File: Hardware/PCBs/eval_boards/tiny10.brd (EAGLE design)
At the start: 12.7 x 17.7 mm, 5 parts, among them IC1 HSDL-9100

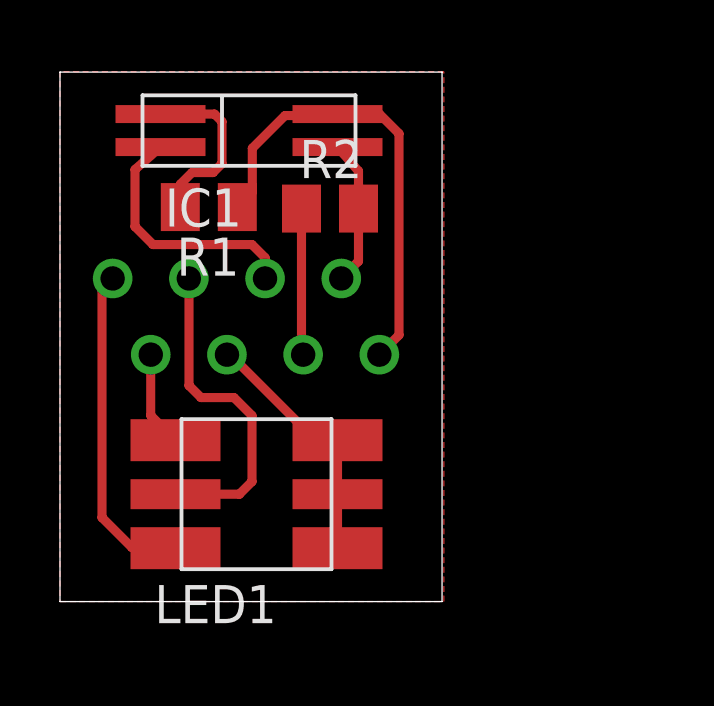
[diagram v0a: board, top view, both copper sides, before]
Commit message: the forgotten commit ;)
* enhance bottom, rgb sensor pcb
* create attiny and lm239 eval boards
* bug fix for the pdf export scripts
* correct attiny soft power switch simulation
* add experimental color sensor code
* add rgb color look up table
* correct motor roations
* various other (this is the forgetten commit)
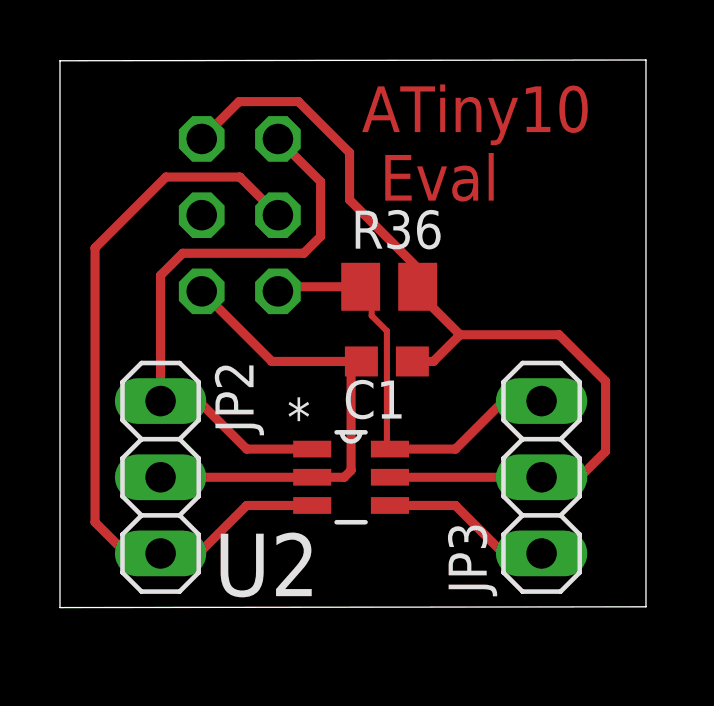
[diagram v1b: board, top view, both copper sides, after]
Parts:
- removed IC1: HSDL-9100, BEEP:HSDL-9100
- removed LED1: F503605050, BEEP:5050LED
- removed R1: (no value), resistor:M0805
- removed R2: 39K, resistor:M0805
- removed X1: (no value), con-amp:FTOP-8
- added C1: 100n, rcl:C0603
- added JP1: (no value), pinhead:2X03
- added JP2, JP3: (no value), pinhead:1X03
- added R36: (no value), rcl:M0805
- added U2: ATTINY10-TSHR, Atmel_By_element14_Batch_1:SOT95P280X145-6N
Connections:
- removed net +5V: IC1.DET_K, R1.1, X1.1
- removed net ADISTANCE: IC1.DET_A, R2.2, X1.2
- removed net IR_LED_K: IC1.LED_K, X1.4
- removed net N$2: IC1.LED_A, R1.2
- removed net RGB_ANODE_1: LED1.B1, X1.8
- removed net RGB_ANODE_2: LED1.G1, X1.6
- removed net RGB_ANODE_3: LED1.R1, X1.7
- removed net RGB_COMMON_K: LED1.B2, LED1.G2, LED1.R2, X1.5
- new net +3V3: C1.1, JP1.2, JP3.2, R36.2, U2.5
- new net PB0/TPIDATA: JP1.1, JP2.1, U2.1
- new net PB1/TPICLK: JP1.3, JP2.3, U2.3
- new net PB2/SOFT_OFF: JP3.1, U2.4
- new net PB3/RESET: JP1.5, JP3.3, R36.1, U2.6
- net GND: now also C1.2, JP1.6, JP2.2, U2.2; no longer R2.1, X1.3
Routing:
- net +3V3: track 0.00 -> 31.4 mm
- net PB1/TPICLK: track 0.00 -> 25.1 mm
- net PB0/TPIDATA: track 0.00 -> 19.6 mm
- net +5V: track 15.4 -> 0.00 mm
- net PB3/RESET: track 0.00 -> 14.4 mm
- net GND: track 4.89 -> 16.5 mm
- net RGB_ANODE_2: track 11.0 -> 0.00 mm
- net RGB_ANODE_1: track 11.0 -> 0.00 mm
- net IR_LED_K: track 8.49 -> 0.00 mm
- net RGB_COMMON_K: track 8.47 -> 0.00 mm
- net N$2: track 5.99 -> 0.00 mm
- net PB2/SOFT_OFF: track 0.00 -> 5.72 mm
- net ADISTANCE: track 4.88 -> 0.00 mm
- net RGB_ANODE_3: track 3.19 -> 0.00 mm
- removed copper zone on layer 1, net GND
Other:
- board size 12.7 x 17.7 mm -> 19.5 x 18.3 mm
- board text added: "ATiny10 Eval"
